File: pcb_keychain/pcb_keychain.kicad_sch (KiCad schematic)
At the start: 2 parts, among them SW1 SW_Push, U1 13.56MHz

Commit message: updated schematic
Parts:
- removed SW1: SW_Push, Button_Switch_Keyboard:SW_Cherry_MX_1.00u_PCB, symbol Switch:SW_Push
- added AE1: Antenna_Loop, symbol Device:Antenna_Loop
- added C1: C, symbol Device:C
- added D1: LED, symbol Device:LED
- added R1: R, symbol Device:R
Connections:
- net at U1.1 (LA): now also AE1.1
- net at U1.2 (VSS): now also C1.1, D1.1 (K)
- net at U1.6 (VCC): now also U1.7 (VOUT), C1.2, R1.2
- net at U1.8 (LB): now also AE1.2
- new net: D1.2 (A), R1.1

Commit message: updated sch
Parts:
- C1: value C -> 220nF
- R1: value R -> 47*
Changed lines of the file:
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@@
 			)
 		)
-		(property "Value" "R"
+		(property "Value" "47*"
 			(at 96.52 77.47 90)
 			(effects
@@
 			)
 		)
-		(property "Value" "C"
+		(property "Value" "220nF"
 			(at 86.36 64.77 90)
 			(effects

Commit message: updated schematic
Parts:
- removed AE1: Antenna_Loop, symbol Device:Antenna_Loop
- removed C1: 220nF, symbol Device:C
- removed U1: 13.56MHz, NT3H2111W0FHKH:XQFN-8_L1.6-W1.6-P0.50-BL, symbol JLC_Imports:NT3H2111W0FHKH
- added BT1: Battery_Cell, symbol Device:Battery_Cell
- added Q1: PN2222A, Package_TO_SOT_THT:TO-92_Inline, symbol Transistor_BJT:PN2222A
- added R2: R_Photo, symbol Device:R_Photo
- added R3: 47k, symbol Device:R
- added SW1: SW_Slide_DPDT, symbol Switch:SW_Slide_DPDT
- R1: value 47* -> 470
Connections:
- net at D1.1 (K): now also R1.1
- net at R1.2: now also Q1.3 (C)
- net at D1.2 (A): now also BT1.1 (+), R3.1; no longer R1.1
- new net: Q1.1 (E), R2.2, SW1.4 (A), SW1.5 (B)
- new net: BT1.2 (-), SW1.6 (C)
- new net: Q1.2 (B), R2.1, R3.2

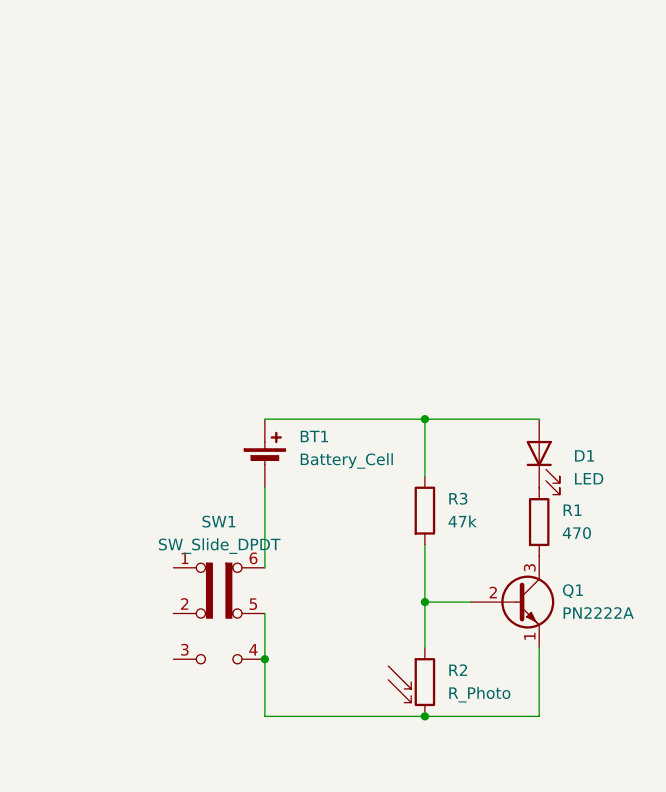
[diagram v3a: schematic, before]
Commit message: updated pcb keychain
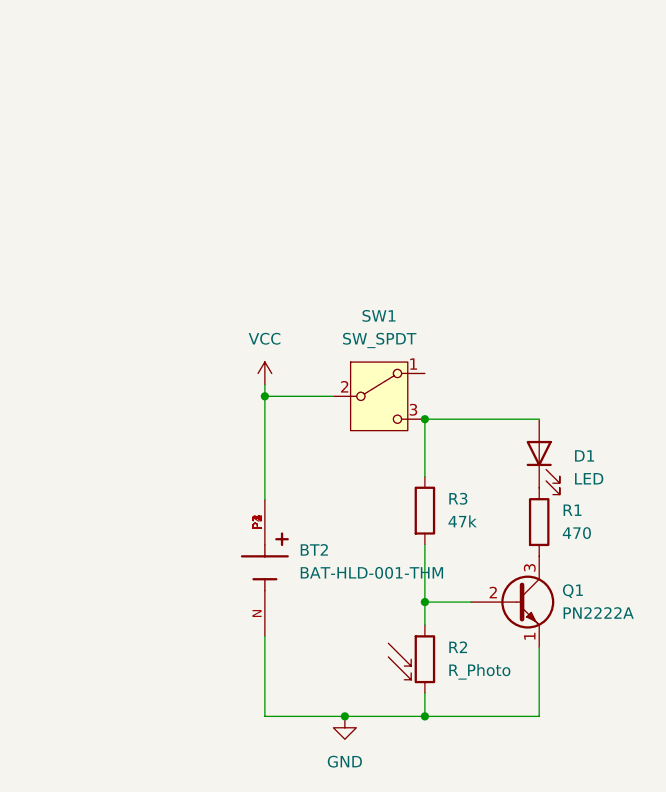
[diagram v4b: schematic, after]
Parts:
- removed BT1: Battery_Cell, symbol Device:Battery_Cell
- removed SW1: SW_Slide_DPDT, symbol Switch:SW_Slide_DPDT
- added BT2: BAT-HLD-001-THM, BAT-HLD-001-THM:BAT_BAT-HLD-001-THM, symbol BAT-HLD-001-THM:BAT-HLD-001-THM
- added SW1: SW_SPDT, Connector_PinSocket_2.54mm:PinSocket_1x03_P2.54mm_Vertical, symbol Switch:SW_SPDT
- D1: footprint (none) -> LED_THT:LED_D8.0mm
- R1, R3: footprint (none) -> Resistor_THT:R_Axial_DIN0207_L6.3mm_D2.5mm_P10.16mm_Horizontal
- R2: footprint (none) -> OptoDevice:R_LDR_5.1x4.3mm_P3.4mm_Vertical
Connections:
- net GND: now reaches Q1.1 (E), R2.2
- net GND: now also BT2.N
- net at D1.2 (A), R3.1: now also SW1.3 (C)
- new net VCC: BT2.P1, BT2.P2, BT2.P3, BT2.P4, SW1.2 (B)
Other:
- moved on the sheet: R2

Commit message: v1 done. holy fk that was a sprint lmao
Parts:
- removed BT2: BAT-HLD-001-THM, BAT-HLD-001-THM:BAT_BAT-HLD-001-THM, symbol BAT-HLD-001-THM:BAT-HLD-001-THM
- removed SW1: SW_SPDT, Connector_PinSocket_2.54mm:PinSocket_1x03_P2.54mm_Vertical, symbol Switch:SW_SPDT
- added BT1: BAT-HLD-001, BAT-HLD-001:BAT_BAT-HLD-001, symbol BAT-HLD-001:BAT-HLD-001
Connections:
- net GND: now also BT1.N1
- net VCC: now also D1.2 (A), R3.1, BT1.P1, BT1.P2
